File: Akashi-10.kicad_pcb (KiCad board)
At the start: 2 copper layers, 66 x 83.5 mm, 14 parts, among them J1 Conn_02x20_Odd_Even, J2 Conn_02x20_Odd_Even, J3 Conn_02x20_Counter_Clockwise, P1 EL-210-KEY, U1 9-ST-20

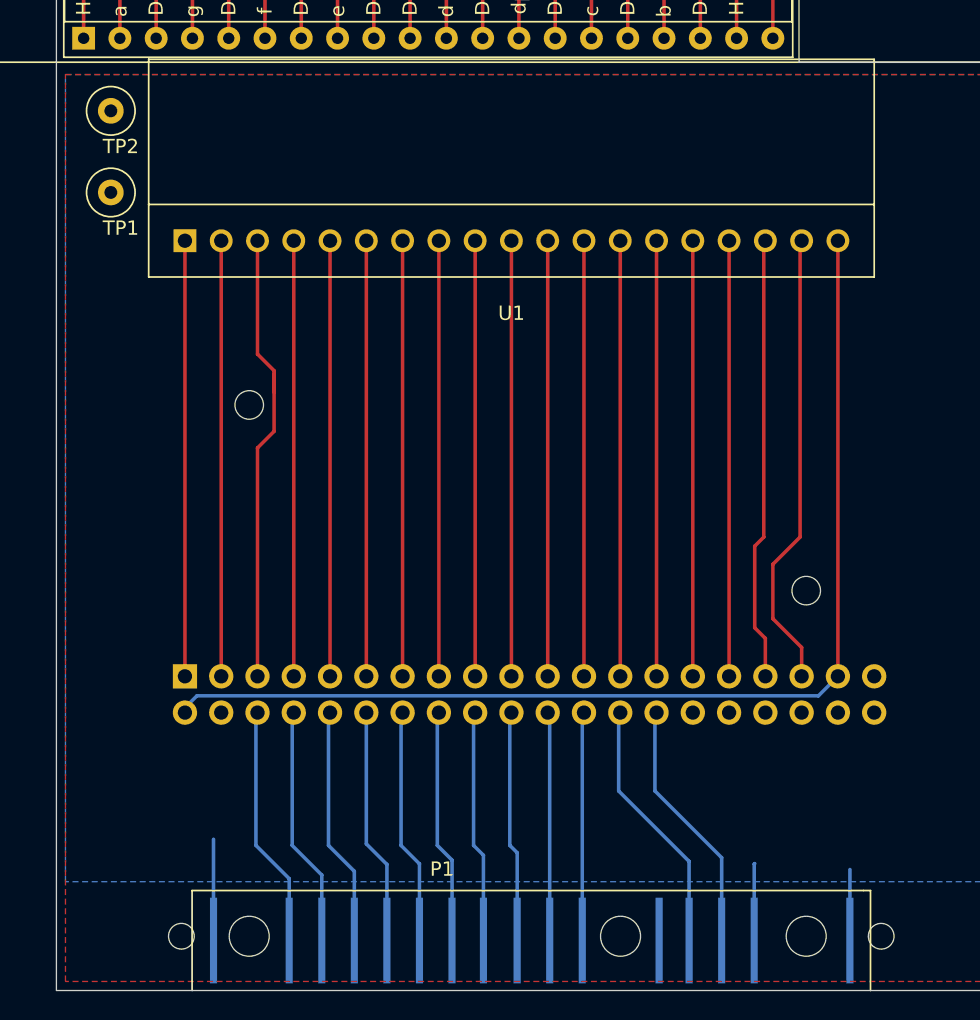
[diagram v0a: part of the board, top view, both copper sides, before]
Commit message: P1 pattern fixed.
Hole size changed. GND/3.3V position changed.
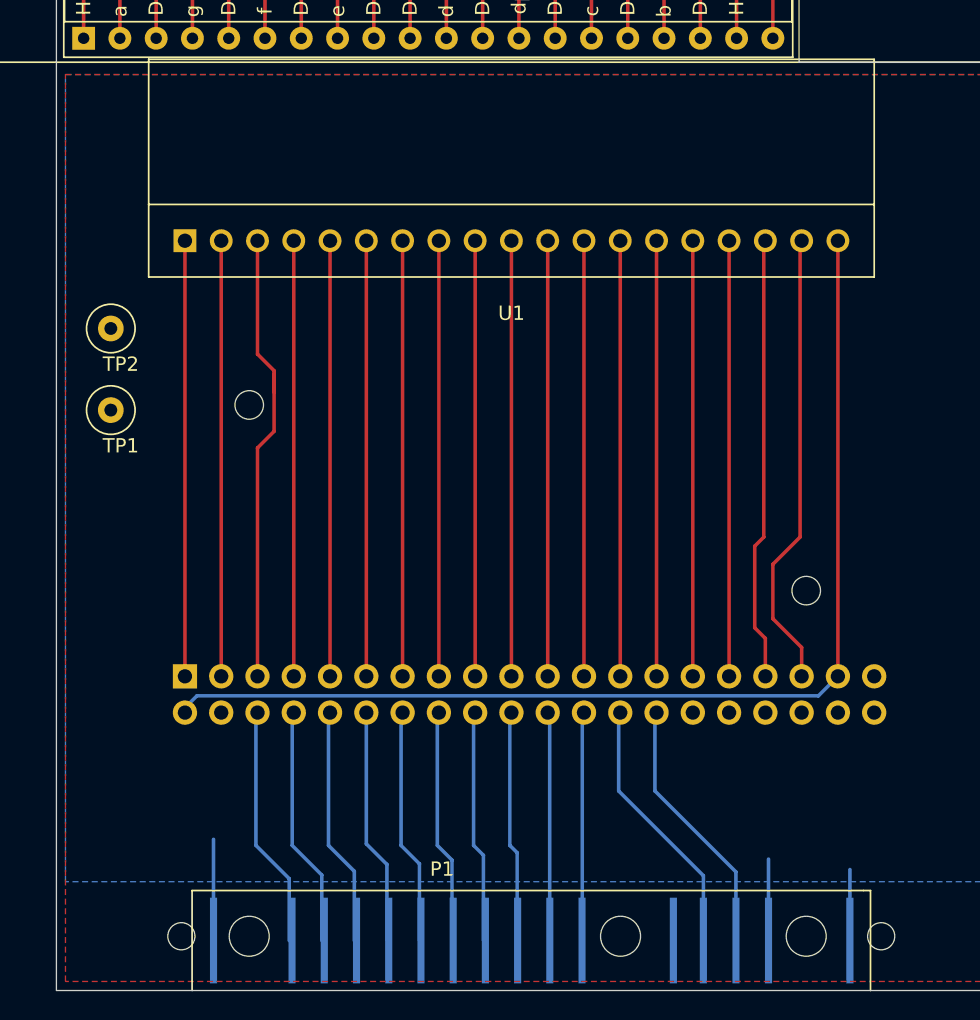
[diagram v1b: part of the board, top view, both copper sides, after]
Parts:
- REF** (x2): value hole_1.8mm -> hole_1.9mm
- moved TP1 15.2 mm to (122.8, 97.4)
- moved TP2 15.2 mm to (122.8, 91.6)
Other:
- board text added: "Akashi-10 v1.0.1"
- board text removed: "Akashi-10 v1.0.0"

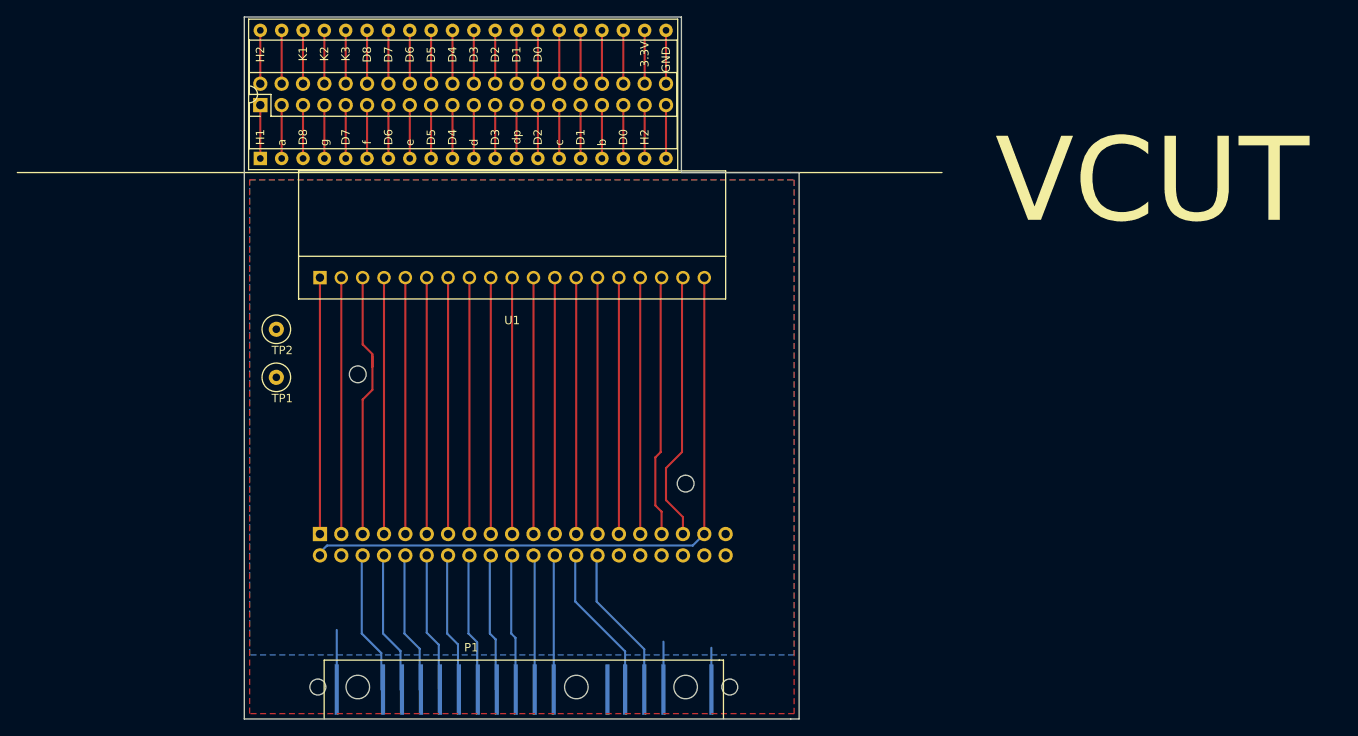
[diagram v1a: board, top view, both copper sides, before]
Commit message: Add lost holes.
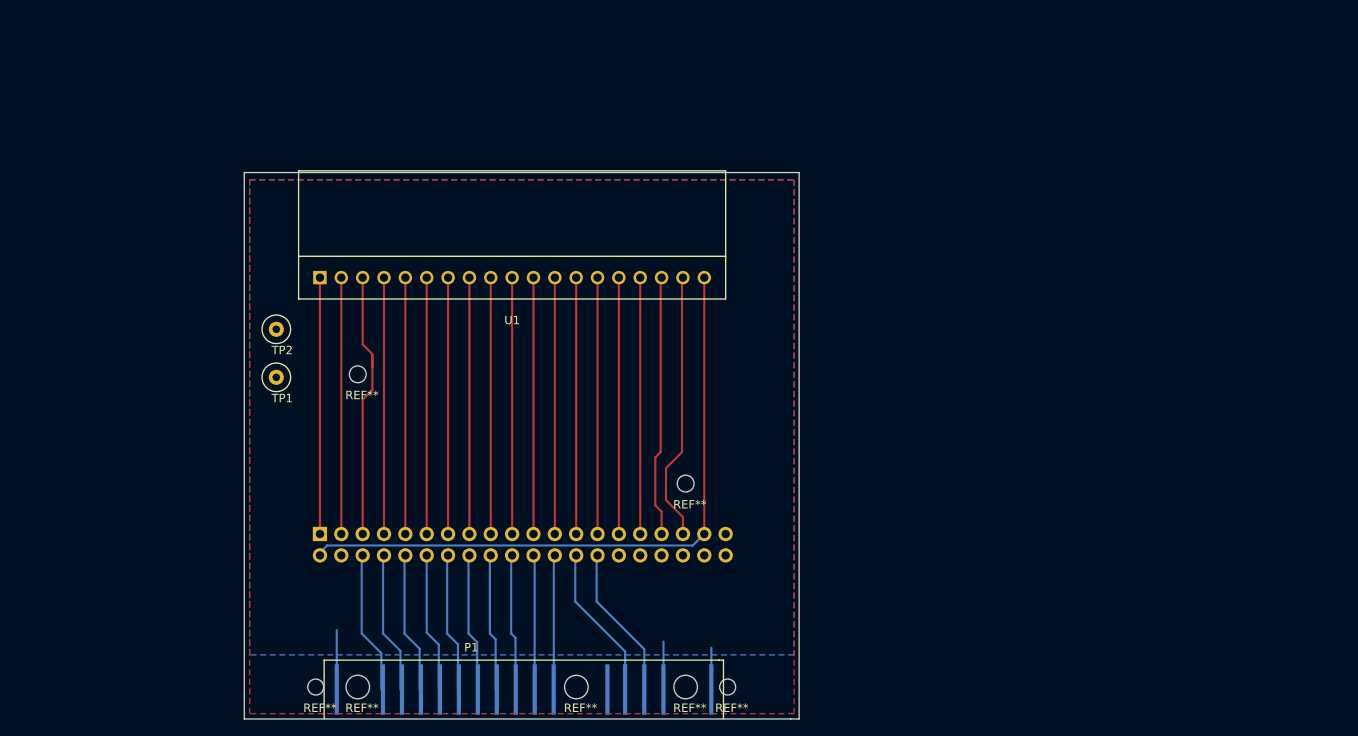
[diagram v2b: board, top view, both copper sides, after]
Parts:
- removed J2: Conn_02x20_Odd_Even, Connector_PinHeader_2.54mm:PinHeader_2x20_P2.54mm_Vertical
- removed J3: Conn_02x20_Counter_Clockwise, Package_DIP:DIP-40_W15.24mm_Socket
- removed the REF** at (176.8, 134.2)
- removed the REF** at (127.8, 134.2)
- added REF**: hole_1.9mm, hole:hole_1.8mm, F.Cu at (176.5, 134.2)
- added REF**: hole_1.9mm, hole:hole_1.8mm, F.Cu at (127.5, 134.2)
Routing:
- net Net-(J2-Pad11): track 7.25 -> 0.00 mm
- net Net-(J2-Pad9): track 6.35 -> 0.00 mm
- net Net-(J2-Pad7): track 6.35 -> 0.00 mm
- net Net-(J2-Pad5): track 6.35 -> 0.00 mm
- net Net-(J2-Pad39): track 6.35 -> 0.00 mm
- net Net-(J2-Pad37): track 6.35 -> 0.00 mm
- net Net-(J2-Pad35): track 6.35 -> 0.00 mm
- net Net-(J2-Pad33): track 6.35 -> 0.00 mm
- net Net-(J2-Pad31): track 6.35 -> 0.00 mm
- net Net-(J2-Pad3): track 6.35 -> 0.00 mm
- net Net-(J2-Pad29): track 6.35 -> 0.00 mm
- net Net-(J2-Pad27): track 6.35 -> 0.00 mm
- net Net-(J2-Pad25): track 6.35 -> 0.00 mm
- net Net-(J2-Pad23): track 6.35 -> 0.00 mm
- net Net-(J2-Pad21): track 6.35 -> 0.00 mm
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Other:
- board size 66 x 83.5 mm -> 66 x 65 mm
- board text added: "Akashi-10 v1.0.2"
- board text removed: "3.3V"
- board text removed: "Akashi-10 v1.0.1"
- board text removed: "D0"
- board text removed: "D1"
- board text removed: "D2"
- board text removed: "D3"
- board text removed: "D4"
- board text removed: "D5"
- board text removed: "D6"
- board text removed: "D7"
- board text removed: "D8"
- board text removed: "H1"
- board text removed: "H2"
- board text removed: "K1"
- board text removed: "K2"
- board text removed: "K3"
- board text removed: "VCUT"
- board text removed: "a"
- board text removed: "b"
- board text removed: "c"
- board text removed: "d"
- board text removed: "dp"
- board text removed: "e"
- board text removed: "f"
- board text removed: "g"
